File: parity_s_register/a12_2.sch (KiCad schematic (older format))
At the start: 22 parts, among them U12026 74HC27, U12028 74HC02, U12029 74HC04, U12030 74HC02, U12031 74HC02, U12032 74HC02, U12033 74HC04, U12034 74HC02, U12035 74HC02, U12036 74HC02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

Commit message: Finished off and integrated module 14. Also fixed a couple of bugs this turned up (both initial conditions, and bad wiring in the CGMC pulse generator and S register)
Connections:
- net CSG: now also U12040.12
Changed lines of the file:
@@
 Text HLabel 12550 3550 0    60   Input ~ 0
 OCTAD2
+Wire Wire Line
+	8200 8500 6650 8500
+Connection ~ 6650 8500
 $EndSCHEMATC

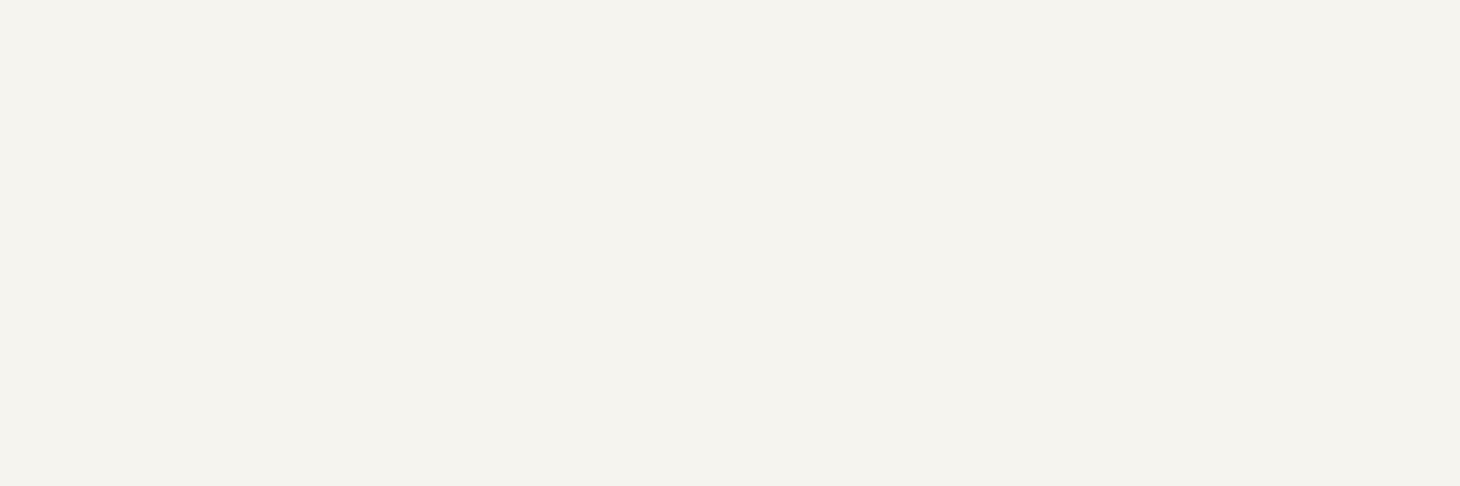
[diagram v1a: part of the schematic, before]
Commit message: Added erasable memory, and fixed lots of random wiring errors.
I decided to go with a 16-bit-wide MRAM chip -- I had  no idea
until I started researching RAM options how technologically
similar MRAM is to core memory. The datasheet diagrams look like
they're straight out of the AGC documentation!

There's a slight inaccuracy in this implementation worth mentioning.
Like fixed memory, I've wired the sense amplifier outputs directly up
to the tristate data output pins of the MRAM chip. But because the
data lines are bidirectional, data being written into RAM will show up
on the sense lines, and go straight into the ungated G register. Since
G is what's being written out, this doesn't matter 99% of the time, but
if there's an overflow condition in G (I don't even know if this is
possible), the bit 16 will be copied over bit 16, and the overflow
condition will be lost. I'll keep an eye out to see if anything relies
on G not changing after the write cycle is complete.

With erasable memory introduced, the computer now theoretically supports
all programs that don't use I/O or interrupts. I've started running
the VirtualAGC validation program, and have been fixing random errors
uncovered by failing self-tests.
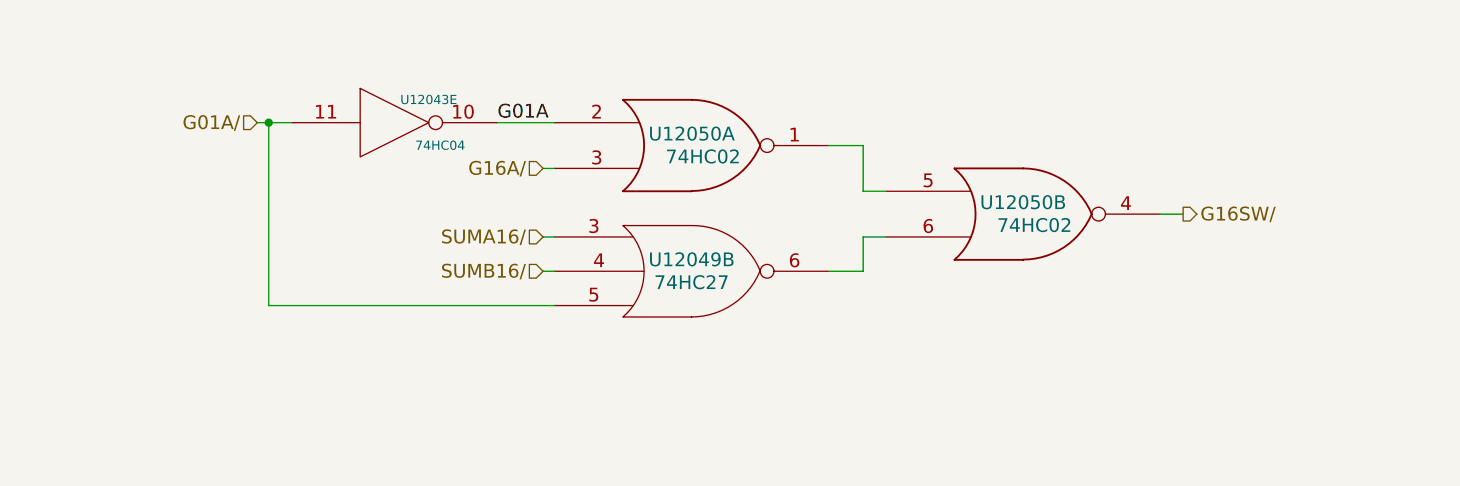
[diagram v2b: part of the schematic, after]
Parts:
- added unit 5 of U12043
- added unit 2 of U12049
- added U12050: 74HC02, symbol 74HC02
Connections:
- net GND: now also U12043.7 (GND), U12049.7 (GND), U12050.7 (GND), U12050.7 (GND)
- net VCC: now also U12043.14 (VCC), U12049.14 (VCC), U12050.14 (VCC), U12050.14 (VCC)
- new net: U12050.1, U12050.5
- new net: U12049.6, U12050.6
- new net G01A: U12043.10, U12050.2
- new net G01A/: U12043.11, U12049.5
- new net G16A/: U12050.3
- new net G16SW/: U12050.4
- new net SUMA16/: U12049.3
- new net SUMB16/: U12049.4
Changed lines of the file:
@@
 	8200 8500 6650 8500
 Connection ~ 6650 8500
+$Comp
+L 74HC02 U12050
+U 1 1 5705E3F4
+P 14900 1400
+F 0 "U12050" H 14900 1450 60  0000 C CNN
+F 1 "74HC02" H 14950 1350 60  0000 C CNN
+F 2 "" H 14900 1400 60  0000 C CNN
+F 3 "" H 14900 1400 60  0000 C CNN
+	1    14900 1400
+	1    0    0    -1
+$EndComp
+$Comp
+L 74HC02 U12050
+U 2 1 5705E608
+P 16350 1700
+F 0 "U12050" H 16350 1750 60  0000 C CNN
+F 1 "74HC02" H 16400 1650 60  0000 C CNN
+F 2 "" H 16350 1700 60  0000 C CNN
+F 3 "" H 16350 1700 60  0000 C CNN
+	2    16350 1700
+	1    0    0    -1
+$EndComp
+Wire Wire Line
+	15500 1400 15650 1400
+Wire Wire Line
+	15650 1400 15650 1600
+Wire Wire Line
+	15650 1600 15750 1600
+Wire Wire Line
+	15750 1800 15650 1800
+Wire Wire Line
+	15650 1800 15650 1950
+Wire Wire Line
+	15650 1950 15500 1950
+$Comp
+L 74HC27 U12049
+U 2 1 5705ECA8
+P 14900 1950
+F 0 "U12049" H 14900 2000 60  0000 C CNN
+F 1 "74HC27" H 14900 1900 60  0000 C CNN
+F 2 "" H 14900 1950 60  0000 C CNN
+F 3 "" H 14900 1950 60  0000 C CNN
+	2    14900 1950
+	1    0    0    -1
+$EndComp
+Wire Wire Line
+	14300 1300 14050 1300
+$Comp
+L 74HC04 U12043
+U 5 1 57061DAA
+P 13600 1300
+F 0 "U12043" H 13750 1400 40  0000 C CNN
+F 1 "74HC04" H 13800 1200 40  0000 C CNN
+F 2 "" H 13600 1300 60  0000 C CNN
+F 3 "" H 13600 1300 60  0000 C CNN
+	5    13600 1300
+	1    0    0    -1
+$EndComp
+Text HLabel 13000 1300 0    60   Input ~ 0
+G01A/
+Wire Wire Line
+	13150 1300 13000 1300
+Text Label 14050 1300 0    60   ~ 0
+G01A
+Wire Wire Line
+	13050 1300 13050 2100
+Wire Wire Line
+	13050 2100 14300 2100
+Connection ~ 13050 1300
+Wire Wire Line
+	14300 1500 14250 1500
+Text HLabel 14250 1500 0    60   Input ~ 0
+G16A/
+Wire Wire Line
+	14300 1800 14250 1800
+Text HLabel 14250 1800 0    60   Input ~ 0
+SUMA16/
+Wire Wire Line
+	14300 1950 14250 1950
+Text HLabel 14250 1950 0    60   Input ~ 0
+SUMB16/
+Wire Wire Line
+	16950 1700 17050 1700
+Text HLabel 17050 1700 2    60   Output ~ 0
+G16SW/
 $EndSCHEMATC

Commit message: Fixed not->1-input nor in the rest of the modules.
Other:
- moved on the sheet: U12029A, U12029B, U12029C, U12029D, U12029E, U12029F, U12033A, U12033B, U12033C, U12033D, U12033E, U12033F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

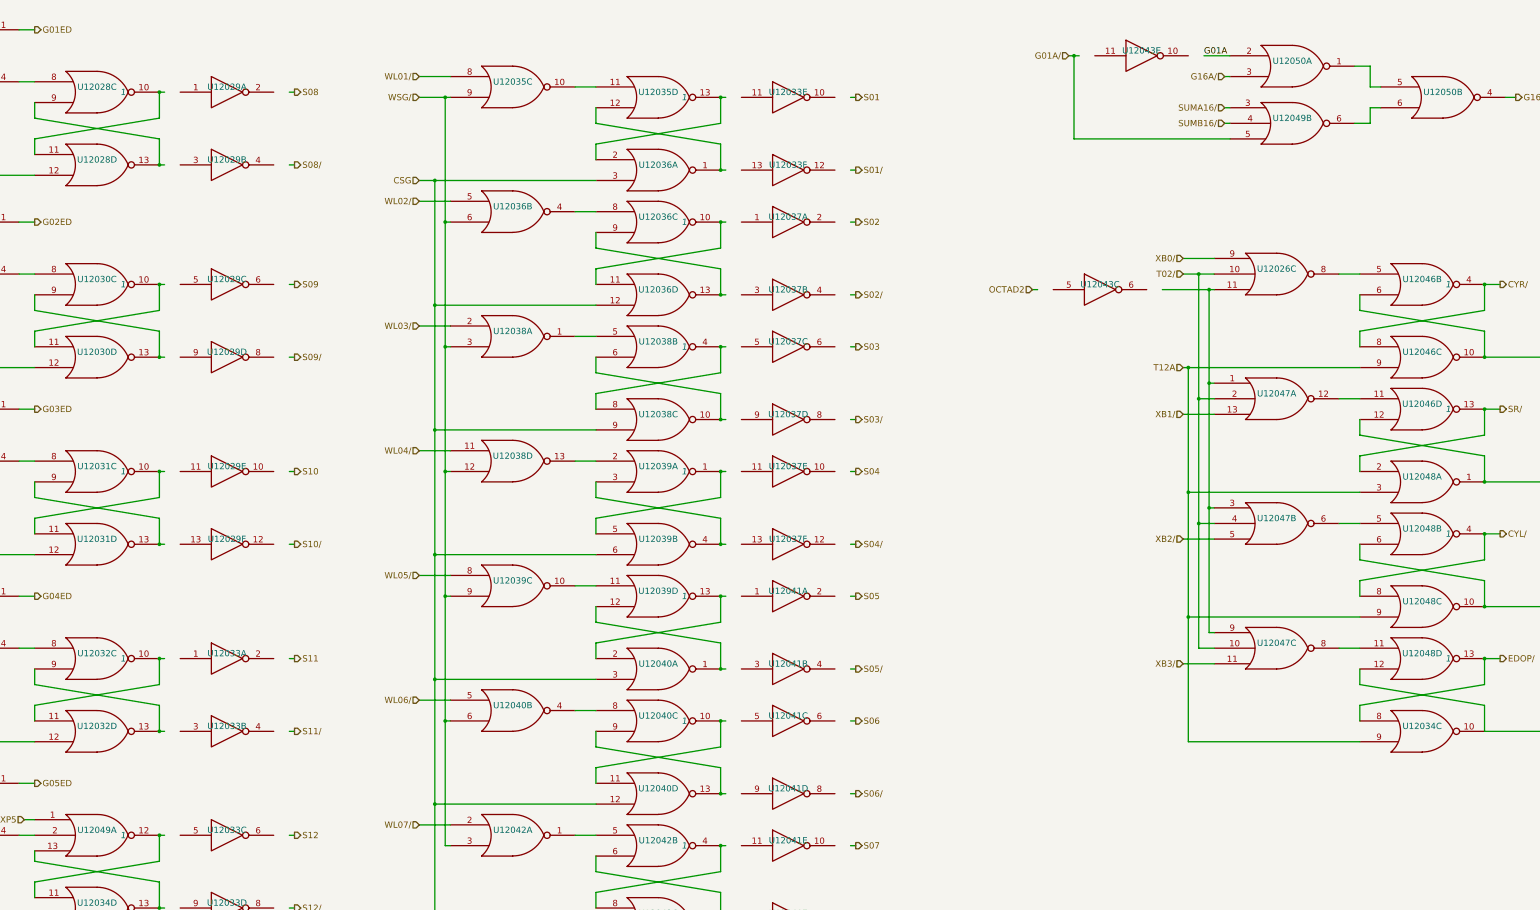
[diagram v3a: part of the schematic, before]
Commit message: Updated Parity and S Register to be on +4VSW
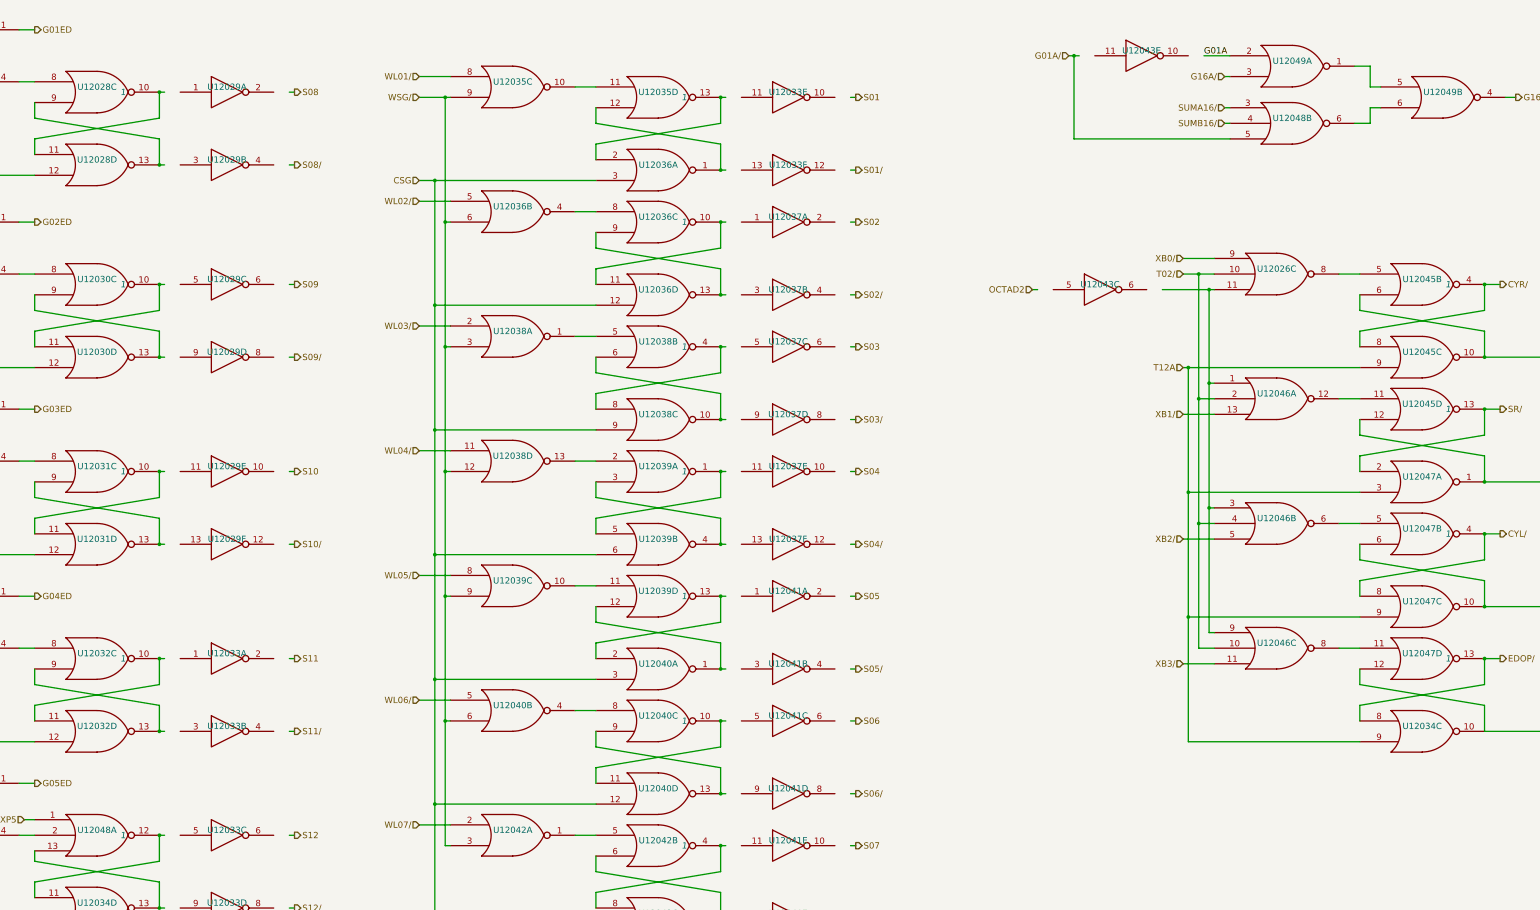
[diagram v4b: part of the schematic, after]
